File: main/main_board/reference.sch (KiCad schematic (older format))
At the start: 8 parts

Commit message: A bunch of thinking about RFI and ESD, and some testing.  Mostly reflected in notebook.txt. Also another more explicit round of consideration of box-level grounding and power distribution, because this affects the power conditioning on the main board.  Power nets on the main board are mostly captured.  I added supply decoupling at each plugin slot.
in_filter.sxsch: added simulation of ESD, use vendor models for TVS diode and ferrite.

power_budget.xlsx: get rid of sheets for the input boards not implemented.  Add sheet for
the main board and carry over data from the input board sheet.
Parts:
- removed C?: 1uF, Capacitor_SMD:C_0805_2012Metric, symbol Device:C_Small
- removed C?: 10uF, Capacitor_SMD:C_0603_1608Metric, symbol Device:C_Small
- removed C?: 330uF, Capacitor_SMD:CP_Elec_8x6.7, symbol Device:CP1_Small
- removed C?: 22 uF, Capacitor_THT:C_Rect_L26.5mm_W11.5mm_P22.50mm_MKS4, symbol Device:C_Small
- removed FB?: 21 Ohm, Inductor_SMD:L_0805_2012Metric, symbol dk_Ferrite-Beads-and-Chips:MPZ2012S601AT000
- removed R?: 200, Resistor_SMD:R_0603_1608Metric, symbol Device:R_US
- removed R?: 1K, Resistor_SMD:R_0603_1608Metric, symbol Device:R_US
- removed U?: NCP1117STAT3G, Package_TO_SOT_SMD:SOT-223, symbol dk_PMIC-Voltage-Regulators-Linear:NCP1117ST33T3G
- added C? (x2): 3.3 uF, Capacitor_THT:C_Rect_L13.0mm_W6.0mm_P10.00mm_FKS3_FKP3_MKS4, symbol Device:C_Small
- added C? (x2): 47uF, Capacitor_SMD:C_1210_3225Metric, symbol Device:C_Small
- added C? (x3): 1uF, Capacitor_SMD:C_0805_2012Metric, symbol Device:C_Small
- added C?: OPT, Capacitor_SMD:C_0603_1608Metric, symbol Device:C_Small
- added C?: bulk >=16V, Capacitor_SMD:C_1210_3225Metric, symbol Device:C_Small
- added FB? (x2): 2K Ohm, Inductor_SMD:L_0805_2012Metric, symbol dk_Ferrite-Beads-and-Chips:MPZ2012S601AT000
- added R?: 40K, Resistor_SMD:R_0603_1608Metric, symbol Device:R_US
- added R? (x2): 0, Resistor_SMD:R_0603_1608Metric, symbol Device:R_US
- added R? (x3): 10, Resistor_SMD:R_0603_1608Metric, symbol Device:R_US
- added U?: MAX6220ASA-5.0+, Package_SO:SOIC-8_3.9x4.9mm_P1.27mm, symbol ilemt_input:MAX6220ASA-5.0+
- added U?: OPA209, Package_SO:SOIC-8_3.9x4.9mm_P1.27mm, symbol ilemt_input:opamp_single
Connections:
- net labels added: -6V
- wire segments 25 -> 57
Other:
- note added: "Master voltage reference and output buffer"
- note removed: "+7.5V"

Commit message: Diffs mainly due to first annotation of some new components.  Also changes on power.sch, added TVS and some caps.
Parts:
- gave numbers to parts that had none: 19
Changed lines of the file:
@@
 AR Path="/5E624B3C/5E2EB92B/5EBF30D8" Ref="C?"  Part="1"
 AR Path="/5EBEDCCA/5EBF30D8" Ref="C?"  Part="1"
-AR Path="/5E525EB8/5EBF30D8" Ref="C?"  Part="1"
-F 0 "C?" V 6821 3350 50  0000 C CNN
+AR Path="/5E525EB8/5EBF30D8" Ref="C5"  Part="1"
+F 0 "C5" V 6821 3350 50  0000 C CNN
 F 1 "3.3 uF" V 6912 3350 50  0000 C CNN
 F 2 "Capacitor_THT:C_Rect_L13.0mm_W6.0mm_P10.00mm_FKS3_FKP3_MKS4" H 7050 3350 50  0001 C CNN
@@
 AR Path="/5E624B3C/5E2EB92B/5EBF5333" Ref="C?"  Part="1"
 AR Path="/5EBEDCCA/5EBF5333" Ref="C?"  Part="1"
-AR Path="/5E525EB8/5EBF5333" Ref="C?"  Part="1"
-F 0 "C?" V 7971 2550 50  0000 C CNN
+AR Path="/5E525EB8/5EBF5333" Ref="C7"  Part="1"
+F 0 "C7" V 7971 2550 50  0000 C CNN
 F 1 "1uF" V 8062 2550 50  0000 C CNN
 F 2 "Capacitor_SMD:C_0805_2012Metric" H 8200 2550 50  0001 C CNN
@@
 AR Path="/5E624B3C/5E2EB92B/5EBF533B" Ref="#PWR?"  Part="1"
 AR Path="/5EBEDCCA/5EBF533B" Ref="#PWR?"  Part="1"
-AR Path="/5E525EB8/5EBF533B" Ref="#PWR?"  Part="1"
-F 0 "#PWR?" H 8450 2300 50  0001 C CNN
+AR Path="/5E525EB8/5EBF533B" Ref="#PWR05"  Part="1"
+F 0 "#PWR05" H 8450 2300 50  0001 C CNN
 F 1 "GNDA" V 8455 2422 50  0000 R CNN
 F 2 "" H 8450 2550 50  0001 C CNN
@@
 AR Path="/5E624B3C/5E2EB92B/5EBF5359" Ref="U?"  Part="1"
 AR Path="/5EBEDCCA/5EBF5359" Ref="U?"  Part="1"
-AR Path="/5E525EB8/5EBF5359" Ref="U?"  Part="1"
-F 0 "U?" H 7950 3200 50  0000 L CNN
+AR Path="/5E525EB8/5EBF5359" Ref="U2"  Part="1"
+F 0 "U2" H 7950 3200 50  0000 L CNN
 F 1 "OPA209" H 7950 3100 50  0000 L CNN
 F 2 "Package_SO:SOIC-8_3.9x4.9mm_P1.27mm" H 7850 3000 50  0001 C CNN
@@
 AR Path="/5E624B3C/5E2EB92B/5EBF6E5A" Ref="C?"  Part="1"
 AR Path="/5EBEDCCA/5EBF6E5A" Ref="C?"  Part="1"
-AR Path="/5E525EB8/5EBF6E5A" Ref="C?"  Part="1"
-F 0 "C?" V 3850 2100 50  0000 C CNN
+AR Path="/5E525EB8/5EBF6E5A" Ref="C3"  Part="1"
+F 0 "C3" V 3850 2100 50  0000 C CNN
 F 1 "bulk >=16V" V 3562 2100 50  0000 C CNN
 F 2 "Capacitor_SMD:C_1210_3225Metric" H 3700 2100 50  0001 C CNN
@@
 P 7850 5250
 AR Path="/5E62FD57/5E630FEC/5EBF8C9C" Ref="#PWR?"  Part="1"
-AR Path="/5E525EB8/5EBF8C9C" Ref="#PWR?"  Part="1"
-F 0 "#PWR?" H 7850 5000 50  0001 C CNN
+AR Path="/5E525EB8/5EBF8C9C" Ref="#PWR04"  Part="1"
+F 0 "#PWR04" H 7850 5000 50  0001 C CNN
 F 1 "GNDA" H 7850 5100 50  0000 C CNN
 F 2 "" H 7850 5250 50  0001 C CNN
@@
 P 3150 4800
 AR Path="/5E62FD57/5E630FEC/5EBF8CA2" Ref="#FLG?"  Part="1"
-AR Path="/5E525EB8/5EBF8CA2" Ref="#FLG?"  Part="1"
-F 0 "#FLG?" H 3150 4875 50  0001 C CNN
+AR Path="/5E525EB8/5EBF8CA2" Ref="#FLG01"  Part="1"
+F 0 "#FLG01" H 3150 4875 50  0001 C CNN
 F 1 "PWR_FLAG" H 3150 4950 50  0000 C CNN
 F 2 "" H 3150 4800 50  0001 C CNN
@@
 AR Path="/5E624B3C/5E2EB92B/5EBF8CB0" Ref="C?"  Part="1"
 AR Path="/5EBEDCCA/5EBF8CB0" Ref="C?"  Part="1"
-AR Path="/5E525EB8/5EBF8CB0" Ref="C?"  Part="1"
-F 0 "C?" V 8000 5050 50  0000 C CNN
+AR Path="/5E525EB8/5EBF8CB0" Ref="C6"  Part="1"
+F 0 "C6" V 8000 5050 50  0000 C CNN
 F 1 "47uF" V 7712 5050 50  0000 C CNN
 F 2 "Capacitor_SMD:C_1210_3225Metric" H 7850 5050 50  0001 C CNN
@@
 P 4350 4300
 AR Path="/5E62FD57/5E630FEC/5EC01D7F" Ref="#PWR?"  Part="1"
-AR Path="/5E525EB8/5EC01D7F" Ref="#PWR?"  Part="1"
-F 0 "#PWR?" H 4350 4050 50  0001 C CNN
+AR Path="/5E525EB8/5EC01D7F" Ref="#PWR03"  Part="1"
+F 0 "#PWR03" H 4350 4050 50  0001 C CNN
 F 1 "GNDA" H 4350 4150 50  0000 C CNN
 F 2 "" H 4350 4300 50  0001 C CNN
@@
 AR Path="/5E62FD57/5E448095/5DE42731/5EBC8F1D" Ref="FB?"  Part="1"
 AR Path="/5E62FD57/5E45936E/5DE42731/5EBC8F1D" Ref="FB?"  Part="1"
-AR Path="/5E525EB8/5EBC8F1D" Ref="FB?"  Part="1"
-F 0 "FB?" H 1750 2137 60  0000 C CNN
+AR Path="/5E525EB8/5EBC8F1D" Ref="FB1"  Part="1"
+F 0 "FB1" H 1750 2137 60  0000 C CNN
 F 1 "2K Ohm" H 1750 2031 60  0000 C CNN
 F 2 "Inductor_SMD:L_0805_2012Metric" H 1950 2050 60  0001 L CNN
@@
 AR Path="/5E62FD57/5E448095/5DE42731/5EBC5800" Ref="FB?"  Part="1"
 AR Path="/5E62FD57/5E45936E/5DE42731/5EBC5800" Ref="FB?"  Part="1"
-AR Path="/5E525EB8/5EBC5800" Ref="FB?"  Part="1"
-F 0 "FB?" H 1750 5087 60  0000 C CNN
+AR Path="/5E525EB8/5EBC5800" Ref="FB2"  Part="1"
+F 0 "FB2" H 1750 5087 60  0000 C CNN
 F 1 "2K Ohm" H 1750 4981 60  0000 C CNN
 F 2 "Inductor_SMD:L_0805_2012Metric" H 1950 5000 60  0001 L CNN
@@
 $EndComp
 $Comp
-L ilemt_input:MAX6220ASA-5.0+ U?
+L ilemt_input:MAX6220ASA-5.0+ U1
 U 1 1 5EBCA843
 P 4650 2650
-F 0 "U?" H 5750 3050 60  0000 C CNN
+F 0 "U1" H 5750 3050 60  0000 C CNN
 F 1 "MAX6220ASA-5.0+" H 5600 2950 60  0000 C CNN
 F 2 "Package_SO:SOIC-8_3.9x4.9mm_P1.27mm" H 5600 2050 60  0001 C CNN
@@
 AR Path="/5E624B3C/5E2EB92B/5EBCDE6E" Ref="C?"  Part="1"
 AR Path="/5EBEDCCA/5EBCDE6E" Ref="C?"  Part="1"
-AR Path="/5E525EB8/5EBCDE6E" Ref="C?"  Part="1"
-F 0 "C?" V 4121 3350 50  0000 C CNN
+AR Path="/5E525EB8/5EBCDE6E" Ref="C4"  Part="1"
+F 0 "C4" V 4121 3350 50  0000 C CNN
 F 1 "3.3 uF" V 4212 3350 50  0000 C CNN
 F 2 "Capacitor_THT:C_Rect_L13.0mm_W6.0mm_P10.00mm_FKS3_FKP3_MKS4" H 4350 3350 50  0001 C CNN
@@
 Connection ~ 4350 4200
 $Comp
-L Device:R_US R?
+L Device:R_US R3
 U 1 1 5EBD4520
 P 6700 2850
-F 0 "R?" V 6800 2850 50  0000 C CNN
+F 0 "R3" V 6800 2850 50  0000 C CNN
 F 1 "40K" V 6600 2850 50  0000 C CNN
 F 2 "Resistor_SMD:R_0603_1608Metric" V 6740 2840 50  0001 C CNN
@@
 AR Path="/5E624B3C/5E2EB92B/5EBD73F5" Ref="C?"  Part="1"
 AR Path="/5EBEDCCA/5EBD73F5" Ref="C?"  Part="1"
-AR Path="/5E525EB8/5EBD73F5" Ref="C?"  Part="1"
-F 0 "C?" V 10100 3500 50  0000 C CNN
+AR Path="/5E525EB8/5EBD73F5" Ref="C9"  Part="1"
+F 0 "C9" V 10100 3500 50  0000 C CNN
 F 1 "47uF" V 9812 3500 50  0000 C CNN
 F 2 "Capacitor_SMD:C_1210_3225Metric" H 9950 3500 50  0001 C CNN
@@
 Connection ~ 4650 4200
 $Comp
-L Device:R_US R?
+L Device:R_US R6
 U 1 1 5EBF0C26
 P 9150 2950
-F 0 "R?" V 9250 2950 50  0000 C CNN
+F 0 "R6" V 9250 2950 50  0000 C CNN
 F 1 "0" V 9050 2950 50  0000 C CNN
 F 2 "Resistor_SMD:R_0603_1608Metric" V 9190 2940 50  0001 C CNN
@@
 $EndComp
 $Comp
-L Device:R_US R?
+L Device:R_US R5
 U 1 1 5EBF1733
 P 8500 3850
-F 0 "R?" V 8600 3850 50  0000 C CNN
+F 0 "R5" V 8600 3850 50  0000 C CNN
 F 1 "0" V 8400 3850 50  0000 C CNN
 F 2 "Resistor_SMD:R_0603_1608Metric" V 8540 3840 50  0001 C CNN
@@
 	7550 3050 7550 3450
 $Comp
-L Device:C_Small C?
+L Device:C_Small C8
 U 1 1 5EBF55C3
 P 8450 3450
-F 0 "C?" V 8600 3400 50  0000 L CNN
+F 0 "C8" V 8600 3400 50  0000 L CNN
 F 1 "OPT" V 8300 3400 50  0000 L CNN
 F 2 "Capacitor_SMD:C_0603_1608Metric" H 8450 3450 50  0001 C CNN
@@
 Master voltage reference and output buffer
 $Comp
-L Device:R_US R?
+L Device:R_US R1
 U 1 1 5EC081C5
 P 2750 1850
-F 0 "R?" V 2850 1850 50  0000 C CNN
+F 0 "R1" V 2850 1850 50  0000 C CNN
 F 1 "10" V 2650 1850 50  0000 C CNN
 F 2 "Resistor_SMD:R_0603_1608Metric" V 2790 1840 50  0001 C CNN
@@
 $EndComp
 $Comp
-L Device:R_US R?
+L Device:R_US R2
 U 1 1 5EC08908
 P 2750 4800
-F 0 "R?" V 2850 4800 50  0000 C CNN
+F 0 "R2" V 2850 4800 50  0000 C CNN
 F 1 "10" V 2650 4800 50  0000 C CNN
 F 2 "Resistor_SMD:R_0603_1608Metric" V 2790 4790 50  0001 C CNN
@@
 	4350 1850 7850 1850
 $Comp
-L Device:R_US R?
+L Device:R_US R4
 U 1 1 5EC237F8
 P 7850 2200
-F 0 "R?" V 7950 2200 50  0000 C CNN
+F 0 "R4" V 7950 2200 50  0000 C CNN
 F 1 "10" V 7750 2200 50  0000 C CNN
 F 2 "Resistor_SMD:R_0603_1608Metric" V 7890 2190 50  0001 C CNN
@@
 P 2350 2300
 AR Path="/5E62FD57/5E630FEC/5ED0636E" Ref="#PWR?"  Part="1"
-AR Path="/5E525EB8/5ED0636E" Ref="#PWR?"  Part="1"
-F 0 "#PWR?" H 2350 2050 50  0001 C CNN
+AR Path="/5E525EB8/5ED0636E" Ref="#PWR01"  Part="1"
+F 0 "#PWR01" H 2350 2050 50  0001 C CNN
 F 1 "GNDA" H 2350 2150 50  0000 C CNN
 F 2 "" H 2350 2300 50  0001 C CNN
@@
 AR Path="/5E624B3C/5E2EB92B/5ED08B32" Ref="C?"  Part="1"
 AR Path="/5EBEDCCA/5ED08B32" Ref="C?"  Part="1"
-AR Path="/5E525EB8/5ED08B32" Ref="C?"  Part="1"
-F 0 "C?" V 2121 2100 50  0000 C CNN
+AR Path="/5E525EB8/5ED08B32" Ref="C1"  Part="1"
+F 0 "C1" V 2121 2100 50  0000 C CNN
 F 1 "1uF" V 2212 2100 50  0000 C CNN
 F 2 "Capacitor_SMD:C_0805_2012Metric" H 2350 2100 50  0001 C CNN
@@
 P 2350 5250
 AR Path="/5E62FD57/5E630FEC/5ED0A96F" Ref="#PWR?"  Part="1"
-AR Path="/5E525EB8/5ED0A96F" Ref="#PWR?"  Part="1"
-F 0 "#PWR?" H 2350 5000 50  0001 C CNN
+AR Path="/5E525EB8/5ED0A96F" Ref="#PWR02"  Part="1"
+F 0 "#PWR02" H 2350 5000 50  0001 C CNN
 F 1 "GNDA" H 2350 5100 50  0000 C CNN
 F 2 "" H 2350 5250 50  0001 C CNN
@@
 AR Path="/5E624B3C/5E2EB92B/5ED0A97B" Ref="C?"  Part="1"
 AR Path="/5EBEDCCA/5ED0A97B" Ref="C?"  Part="1"
-AR Path="/5E525EB8/5ED0A97B" Ref="C?"  Part="1"
-F 0 "C?" V 2121 5050 50  0000 C CNN
+AR Path="/5E525EB8/5ED0A97B" Ref="C2"  Part="1"
+F 0 "C2" V 2121 5050 50  0000 C CNN
 F 1 "1uF" V 2212 5050 50  0000 C CNN
 F 2 "Capacitor_SMD:C_0805_2012Metric" H 2350 5050 50  0001 C CNN

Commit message: Schematic is mostly complete (except for BIST DACs), and passes ERC.  Rough placement of components on PCB.
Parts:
- added R12: 0, Resistor_SMD:R_0603_1608Metric, symbol Device:R_US
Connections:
- net labels added: GND
- net labels removed: GNDA
- wire segments 57 -> 60
- no-connect marks 0 -> 1
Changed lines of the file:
@@
 	1550 1850 1400 1850
-$Comp
-L power:GNDA #PWR?
-U 1 1 5E646C1A
-P 3700 2300
-AR Path="/5E62FD57/5E630FEC/5E646C1A" Ref="#PWR?"  Part="1"
-AR Path="/5E525EB8/5E646C1A" Ref="#PWR0102"  Part="1"
-F 0 "#PWR0102" H 3700 2050 50  0001 C CNN
-F 1 "GNDA" H 3700 2150 50  0000 C CNN
-F 2 "" H 3700 2300 50  0001 C CNN
-F 3 "" H 3700 2300 50  0001 C CNN
-	1    3700 2300
-	1    0    0    -1
-$EndComp
 $Comp
 L power:PWR_FLAG #FLG?
@@
 Wire Wire Line
 	7850 2550 7850 2650
-$Comp
-L power:GNDA #PWR?
-U 1 1 5EBF533B
-P 8450 2550
-AR Path="/5DFF6C0D/5EBF533B" Ref="#PWR?"  Part="1"
-AR Path="/5E1D6729/5E1DA2AA/5EBF533B" Ref="#PWR?"  Part="1"
-AR Path="/5E2EB92B/5EBF533B" Ref="#PWR?"  Part="1"
-AR Path="/5E624B3C/5E2EB92B/5EBF533B" Ref="#PWR?"  Part="1"
-AR Path="/5EBEDCCA/5EBF533B" Ref="#PWR?"  Part="1"
-AR Path="/5E525EB8/5EBF533B" Ref="#PWR05"  Part="1"
-F 0 "#PWR05" H 8450 2300 50  0001 C CNN
-F 1 "GNDA" V 8455 2422 50  0000 R CNN
-F 2 "" H 8450 2550 50  0001 C CNN
-F 3 "" H 8450 2550 50  0001 C CNN
-	1    8450 2550
-	0    -1   -1   0
-$EndComp
 Wire Wire Line
 	8300 2550 8450 2550
@@
 	1550 4800 1400 4800
 $Comp
-L power:GNDA #PWR?
-U 1 1 5EBF8C9C
-P 7850 5250
-AR Path="/5E62FD57/5E630FEC/5EBF8C9C" Ref="#PWR?"  Part="1"
-AR Path="/5E525EB8/5EBF8C9C" Ref="#PWR04"  Part="1"
-F 0 "#PWR04" H 7850 5000 50  0001 C CNN
-F 1 "GNDA" H 7850 5100 50  0000 C CNN
-F 2 "" H 7850 5250 50  0001 C CNN
-F 3 "" H 7850 5250 50  0001 C CNN
-	1    7850 5250
-	1    0    0    -1
-$EndComp
-$Comp
 L power:PWR_FLAG #FLG?
 U 1 1 5EBF8CA2
@@
 Wire Wire Line
 	7050 4200 7050 3450
-$Comp
-L power:GNDA #PWR?
-U 1 1 5EC01D7F
-P 4350 4300
-AR Path="/5E62FD57/5E630FEC/5EC01D7F" Ref="#PWR?"  Part="1"
-AR Path="/5E525EB8/5EC01D7F" Ref="#PWR03"  Part="1"
-F 0 "#PWR03" H 4350 4050 50  0001 C CNN
-F 1 "GNDA" H 4350 4150 50  0000 C CNN
-F 2 "" H 4350 4300 50  0001 C CNN
-F 3 "" H 4350 4300 50  0001 C CNN
-	1    4350 4300
-	1    0    0    -1
-$EndComp
 $Comp
 L dk_Ferrite-Beads-and-Chips:MPZ2012S601AT000 FB?
@@
 	7850 1850 7850 2050
 Wire Wire Line
-	7850 2350 7850 2550
+	7850 2350 7850 2450
 Connection ~ 7850 2550
 Connection ~ 9950 2950
-Connection ~ 9950 4200
 Wire Wire Line
 	9950 2950 10400 2950
 Wire Wire Line
-	9950 4200 10400 4200
-Wire Wire Line
 	3150 1850 3700 1850
 Wire Wire Line
@@
 Wire Wire Line
 	2350 2200 2350 2300
-$Comp
-L power:GNDA #PWR?
-U 1 1 5ED0636E
-P 2350 2300
-AR Path="/5E62FD57/5E630FEC/5ED0636E" Ref="#PWR?"  Part="1"
-AR Path="/5E525EB8/5ED0636E" Ref="#PWR01"  Part="1"
-F 0 "#PWR01" H 2350 2050 50  0001 C CNN
-F 1 "GNDA" H 2350 2150 50  0000 C CNN
-F 2 "" H 2350 2300 50  0001 C CNN
-F 3 "" H 2350 2300 50  0001 C CNN
-	1    2350 2300
-	1    0    0    -1
-$EndComp
 Wire Wire Line
 	1950 1850 2350 1850
@@
 Wire Wire Line
 	2350 5150 2350 5250
-$Comp
-L power:GNDA #PWR?
-U 1 1 5ED0A96F
-P 2350 5250
-AR Path="/5E62FD57/5E630FEC/5ED0A96F" Ref="#PWR?"  Part="1"
-AR Path="/5E525EB8/5ED0A96F" Ref="#PWR02"  Part="1"
-F 0 "#PWR02" H 2350 5000 50  0001 C CNN
-F 1 "GNDA" H 2350 5100 50  0000 C CNN
-F 2 "" H 2350 5250 50  0001 C CNN
-F 3 "" H 2350 5250 50  0001 C CNN
-	1    2350 5250
-	1    0    0    -1
-$EndComp
 Wire Wire Line
 	2350 4950 2350 4800
@@
 Connection ~ 3700 1850
 Connection ~ 4350 1850
+$Comp
+L power:PWR_FLAG #FLG?
+U 1 1 5EE6B039
+P 7650 2450
+AR Path="/5E624B3C/5E51E83D/5EE6B039" Ref="#FLG?"  Part="1"
+AR Path="/5E525F2C/5EE6B039" Ref="#FLG?"  Part="1"
+AR Path="/5E525FC9/5EE6B039" Ref="#FLG?"  Part="1"
+AR Path="/5E525EB8/5EE6B039" Ref="#FLG0102"  Part="1"
+F 0 "#FLG0102" H 7650 2525 50  0001 C CNN
+F 1 "PWR_FLAG" V 7750 2500 50  0000 C CNN
+F 2 "" H 7650 2450 50  0001 C CNN
+F 3 "~" H 7650 2450 50  0001 C CNN
+	1    7650 2450
+	0    -1   -1   0
+$EndComp
+Wire Wire Line
+	7650 2450 7850 2450
+Connection ~ 7850 2450
+Wire Wire Line
+	7850 2450 7850 2550
+NoConn ~ 6400 2950
+$Comp
+L Device:R_US R12
+U 1 1 5F668E16
+P 10150 4200
+F 0 "R12" V 10250 4200 50  0000 C CNN
+F 1 "0" V 10050 4200 50  0000 C CNN
+F 2 "Resistor_SMD:R_0603_1608Metric" V 10190 4190 50  0001 C CNN
+F 3 "~" H 10150 4200 50  0001 C CNN
+	1    10150 4200
+	0    1    1    0
+$EndComp
+Wire Wire Line
+	10000 4200 9950 4200
+Connection ~ 9950 4200
+Wire Wire Line
+	10300 4200 10400 4200
+$Comp
+L power:GND #PWR02
+U 1 1 5F69F5B9
+P 2350 5250
+F 0 "#PWR02" H 2350 5000 50  0001 C CNN
+F 1 "GND" H 2350 5100 50  0000 C CNN
+F 2 "" H 2350 5250 50  0001 C CNN
+F 3 "" H 2350 5250 50  0001 C CNN
+	1    2350 5250
+	1    0    0    -1
+$EndComp
+$Comp
+L power:GND #PWR078
+U 1 1 5F69FB0E
+P 7850 5250
+F 0 "#PWR078" H 7850 5000 50  0001 C CNN
+F 1 "GND" H 7850 5100 50  0000 C CNN
+F 2 "" H 7850 5250 50  0001 C CNN
+F 3 "" H 7850 5250 50  0001 C CNN
+	1    7850 5250
+	1    0    0    -1
+$EndComp
+$Comp
+L power:GND #PWR04
+U 1 1 5F69FE7B
+P 4350 4300
+F 0 "#PWR04" H 4350 4050 50  0001 C CNN
+F 1 "GND" H 4350 4150 50  0000 C CNN
+F 2 "" H 4350 4300 50  0001 C CNN
+F 3 "" H 4350 4300 50  0001 C CNN
+	1    4350 4300
+	1    0    0    -1
+$EndComp
+$Comp
+L power:GND #PWR01
+U 1 1 5F6A0363
+P 2350 2300
+F 0 "#PWR01" H 2350 2050 50  0001 C CNN
+F 1 "GND" H 2350 2150 50  0000 C CNN
+F 2 "" H 2350 2300 50  0001 C CNN
+F 3 "" H 2350 2300 50  0001 C CNN
+	1    2350 2300
+	1    0    0    -1
+$EndComp
+$Comp
+L power:GND #PWR03
+U 1 1 5F6A0811
+P 3700 2300
+F 0 "#PWR03" H 3700 2050 50  0001 C CNN
+F 1 "GND" H 3700 2150 50  0000 C CNN
+F 2 "" H 3700 2300 50  0001 C CNN
+F 3 "" H 3700 2300 50  0001 C CNN
+	1    3700 2300
+	1    0    0    -1
+$EndComp
+$Comp
+L power:GND #PWR0102
+U 1 1 5F6A2624
+P 8450 2550
+F 0 "#PWR0102" H 8450 2300 50  0001 C CNN
+F 1 "GND" H 8450 2400 50  0000 C CNN
+F 2 "" H 8450 2550 50  0001 C CNN
+F 3 "" H 8450 2550 50  0001 C CNN
+	1    8450 2550
+	0    -1   -1   0
+$EndComp
 $EndSCHEMATC

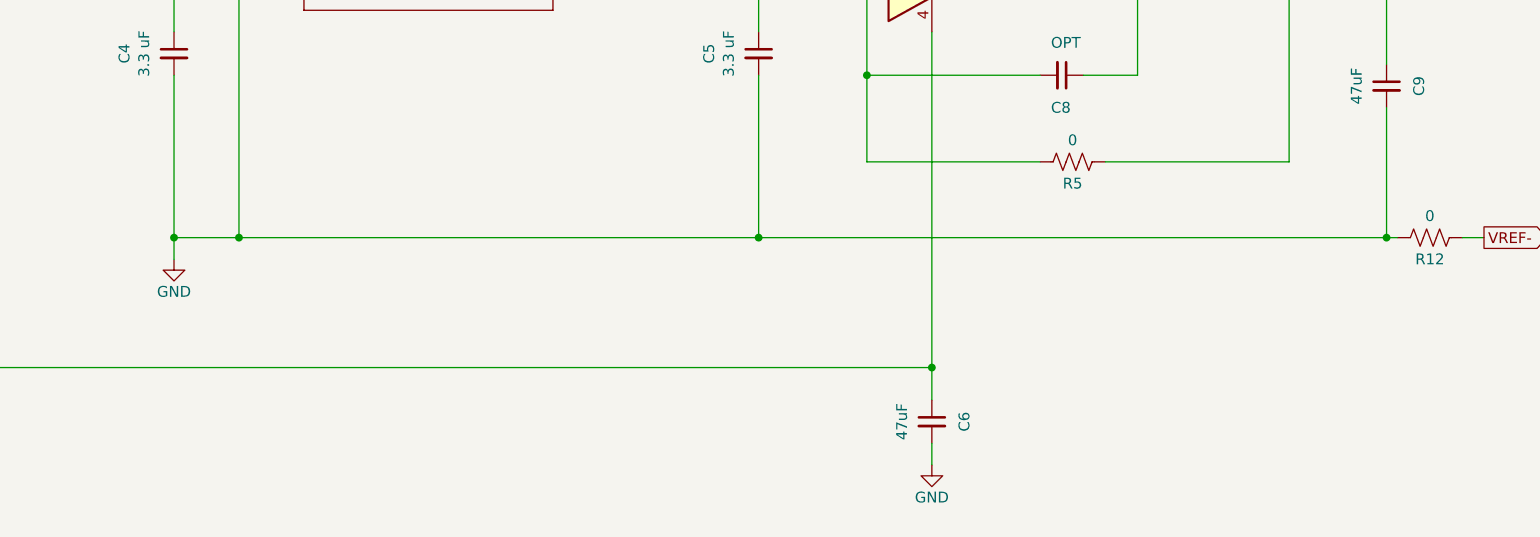
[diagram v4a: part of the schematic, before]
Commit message: Changes related to pin mapping. There's a new BIST unit in the Microzed symbol, and the unit ordering has changed. I also added SDI lines to the input slots which could be used to configure the ADC in a future version of the input board. Added some wire labels for easier routing.
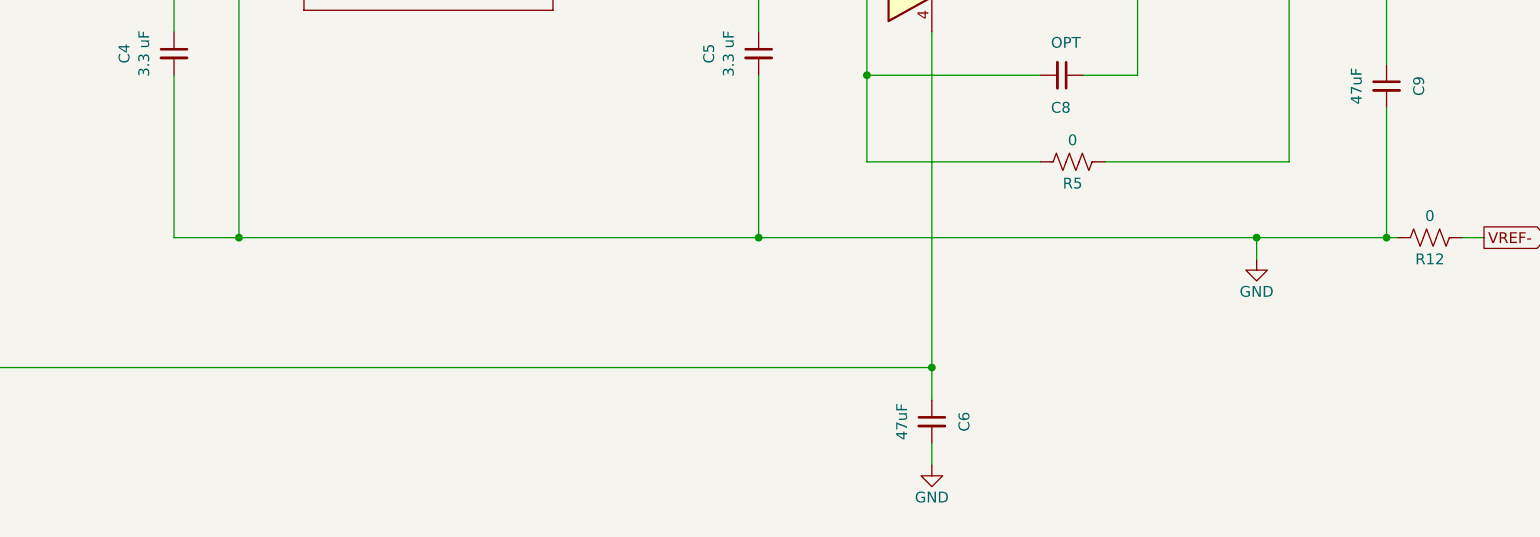
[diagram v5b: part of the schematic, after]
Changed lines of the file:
@@
 Wire Wire Line
 	4350 4200 4650 4200
-Wire Wire Line
-	4350 4300 4350 4200
-Connection ~ 4350 4200
 $Comp
 L Device:R_US R3
@@
 Connection ~ 8800 2950
 Wire Wire Line
-	7050 4200 9950 4200
+	7050 4200 9350 4200
 Wire Wire Line
 	4650 4200 7050 4200
@@
 L power:GND #PWR04
 U 1 1 5F69FE7B
-P 4350 4300
-F 0 "#PWR04" H 4350 4050 50  0001 C CNN
-F 1 "GND" H 4350 4150 50  0000 C CNN
-F 2 "" H 4350 4300 50  0001 C CNN
-F 3 "" H 4350 4300 50  0001 C CNN
-	1    4350 4300
+P 9350 4300
+F 0 "#PWR04" H 9350 4050 50  0001 C CNN
+F 1 "GND" H 9350 4150 50  0000 C CNN
+F 2 "" H 9350 4300 50  0001 C CNN
+F 3 "" H 9350 4300 50  0001 C CNN
+	1    9350 4300
 	1    0    0    -1
 $EndComp
@@
 	0    -1   -1   0
 $EndComp
+Wire Wire Line
+	9350 4300 9350 4200
+Connection ~ 9350 4200
+Wire Wire Line
+	9350 4200 9950 4200
 $EndSCHEMATC
